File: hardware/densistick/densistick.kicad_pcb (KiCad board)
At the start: 4 copper layers, 85 x 22 mm, 66 parts, among them J1 Cable, SW1 SW_Push, U1 TSL2585, U2 USBLC6-2SC6, U3 MIC4812, U4 FT260Q, U5 MIC5365-1.8YC5, U6 CAT24C08, U7 MCP4017-104E/LT

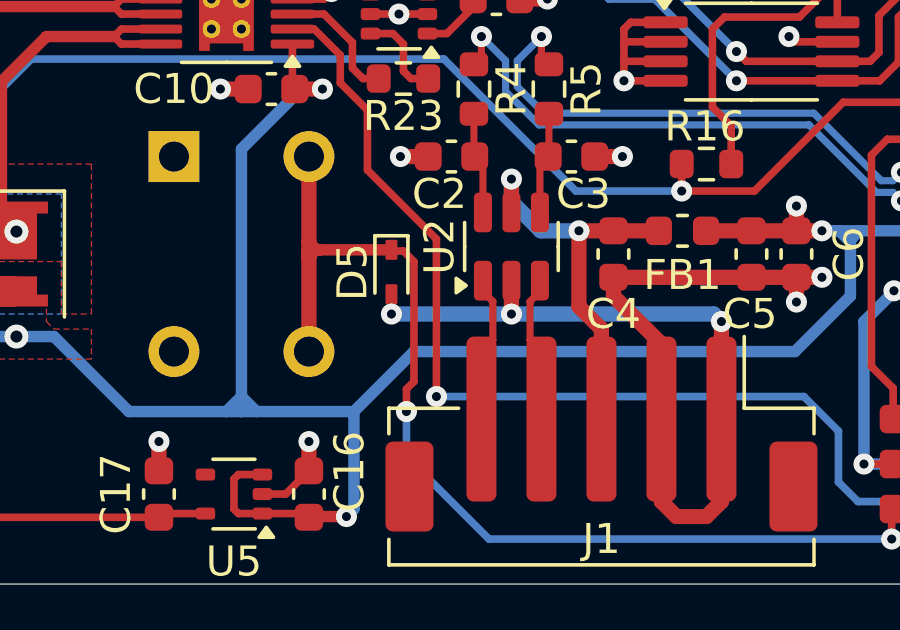
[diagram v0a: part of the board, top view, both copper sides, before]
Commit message: Update ESD diode symbols and footprints
Fix #78
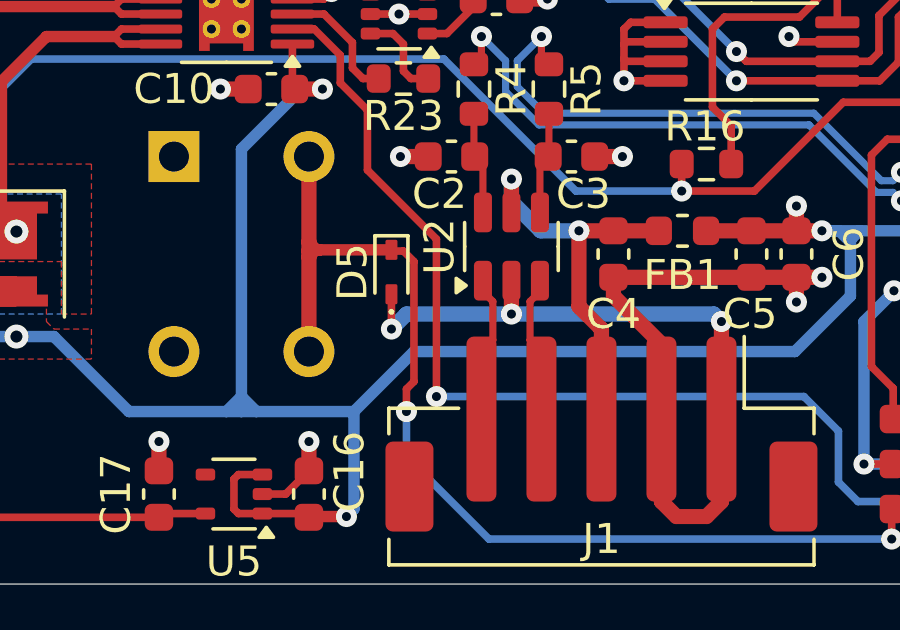
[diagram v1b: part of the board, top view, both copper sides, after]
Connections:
- D5 pad 1: Net-(D5-K) -> Earth
- D5 pad 2: Earth -> Net-(D5-K)
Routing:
- net Earth: track 19.6 -> 20.3 mm
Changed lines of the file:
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@@
 		(layer "F.Cu")
 		(at 88 68.6 -90)
-		(descr "https://www.ti.com/lit/ml/mpss124a/mpss124a.pdf")
+		(descr "https://www.ti.com/lit/ml/mpss124a/mpss124a.pdf, anode and cathod pins reversed")
 		(tags "Diode SOD523 TI DYA0002A")
 		(property "Reference" "D5"
@@
 			)
 		)
-		(property "Datasheet" "https://www.ti.com/lit/ds/slvsen8b/slvsen8b.pdf"
+		(property "Datasheet" "https://www.ti.com/lit/ds/symlink/esd321.pdf"
 			(at 0 0 -90)
 			(unlocked yes)
@@
 		(sheetname "Root")
 		(sheetfile "densistick.kicad_sch")
-		(solder_paste_margin -0.025)
 		(attr smd)
 		(fp_line
@@
 			(layer "F.SilkS")
 		)
+		(fp_circle
+			(center 1.325 0)
+			(end 1.375 0)
+			(stroke
+				(width 0.1)
+				(type solid)
+			)
+			(fill none)
+			(layer "F.SilkS")
+		)
 		(fp_line
 			(start -1.25 0.65)
@@
 		)
 		(pad "1" smd roundrect
-			(at -0.74 0 90)
+			(at 0.74 0 90)
 			(size 0.67 0.4)
 			(layers "F.Cu" "F.Paste" "F.Mask")
 			(roundrect_rratio 0.125)
-			(net 7 "Net-(D5-K)")
-			(pinfunction "K")
+			(net 21 "Earth")
+			(pinfunction "A")
 			(pintype "passive")
 		)
 		(pad "2" smd roundrect
-			(at 0.74 0 90)
+			(at -0.74 0 90)
 			(size 0.67 0.4)
 			(layers "F.Cu" "F.Paste" "F.Mask")
 			(roundrect_rratio 0.125)
-			(net 21 "Earth")
-			(pinfunction "A")
+			(net 7 "Net-(D5-K)")
+			(pinfunction "K")
 			(pintype "passive")
 		)
@@
 			)
 			(rotate
-				(xyz 0 0 0)
+				(xyz 0 0 -180)
 			)
 		)
@@
 		(layer "F.Cu")
 		(at 88.25 60 180)
-		(descr "SOT-363, SC-70-6")
-		(tags "SOT-363 SC-70-6")
+		(descr "SOT-363, SC-70-6, SC-88")
+		(tags "SOT-363 SC-70-6 SC-88")
 		(property "Reference" "U7"
 			(at 0 2 0)
@@
 		(layer "F.Cu")
 		(at 92 67.75 90)
-		(descr "SOT, 6 Pin (https://www.jedec.org/sites/default/files/docs/Mo-178c.PDF variant AB), generated with kicad-footprint-generator ipc_gullwing_generator.py")
+		(descr "SOT, 6 Pin (~), generated with kicad-footprint-generator ipc_gullwing_generator.py")
 		(tags "SOT TO_SOT_SMD")
 		(property "Reference" "U2"
@@
 	(segment
 		(start 88 69.34)
-		(end 88 70)
+		(end 88 70.5)
 		(width 0.254)
 		(layer "F.Cu")
@@
 	)
 	(via
-		(at 88 70)
+		(at 88 70.5)
 		(size 0.7)
 		(drill 0.3)
@@
 	)
 	(segment
-		(start 88 70)
-		(end 92 70)
+		(start 88 70.5)
+		(end 88.5 70)
 		(width 0.508)
 		(layer "B.Cu")
@@
 	)
 	(segment
+		(start 88.5 70)
+		(end 92 70)
+		(width 0.508)
+		(layer "B.Cu")
+		(net 21)
+	)
+	(segment
 		(start 92 70)
 		(end 98.75 70)
@@
 	)
 	(zone
-		(net 7)
-		(net_name "Net-(D5-K)")
+		(net 6)
+		(net_name "/RLED2")
 		(layer "F.Cu")
-		(name "$teardrop_padvia$")
-		(hatch full 0.1)
-		(priority 30001)
-		(attr
-			(teardrop
-				(type padvia)
-			)
-		)
+		(hatch edge 0.5)
+		(priority 6)
 		(connect_pads yes
-			(clearance 0)
+			(clearance 0.508)
 		)
-		(min_thickness 0.0254)
+		(min_thickness 0.25)
 		(filled_areas_thickness no)
 		(fill yes
 			(thermal_gap 0.5)
 			(thermal_bridge_width 0.5)
-			(island_removal_mode 1)
-			(island_area_min 10)
 		)
 		(polygon
 			(pts
-				(xy 84.996 66.45) (xy 85.504 66.45) (xy 86.035298 65.075281) (xy 85.25 64.749) (xy 84.464702 65.075281)
+				(xy 77 70) (xy 78 70) (xy 78 65) (xy 72 65) (xy 72 70) (xy 73 70) (xy 73 68.25) (xy 77 68.25)
 			)
 		)
 	)
 	(zone
-		(net 6)
-		(net_name "/RLED2")
+		(net 7)
+		(net_name "Net-(D5-K)")
 		(layer "F.Cu")
-		(hatch edge 0.5)
-		(priority 6)
+		(name "$teardrop_padvia$")
+		(hatch full 0.1)
+		(priority 30000)
+		(attr
+			(teardrop
+				(type padvia)
+			)
+		)
 		(connect_pads yes
-			(clearance 0.508)
+			(clearance 0)
 		)
-		(min_thickness 0.25)
+		(min_thickness 0.0254)
 		(filled_areas_thickness no)
 		(fill yes
 			(thermal_gap 0.5)
 			(thermal_bridge_width 0.5)
+			(island_removal_mode 1)
+			(island_area_min 10)
 		)
 		(polygon
 			(pts
-				(xy 77 70) (xy 78 70) (xy 78 65) (xy 72 65) (xy 72 70) (xy 73 70) (xy 73 68.25) (xy 77 68.25)
+				(xy 85.504 69.55) (xy 84.996 69.55) (xy 84.464702 70.924719) (xy 85.25 71.251) (xy 86.035298 70.924719)
 			)
 		)
@@
 		(name "$teardrop_padvia$")
 		(hatch full 0.1)
-		(priority 30000)
+		(priority 30001)
 		(attr
 			(teardrop
@@
 		(polygon
 			(pts
-				(xy 85.504 69.55) (xy 84.996 69.55) (xy 84.464702 70.924719) (xy 85.25 71.251) (xy 86.035298 70.924719)
+				(xy 84.996 66.45) (xy 85.504 66.45) (xy 86.035298 65.075281) (xy 85.25 64.749) (xy 84.464702 65.075281)
 			)
 		)

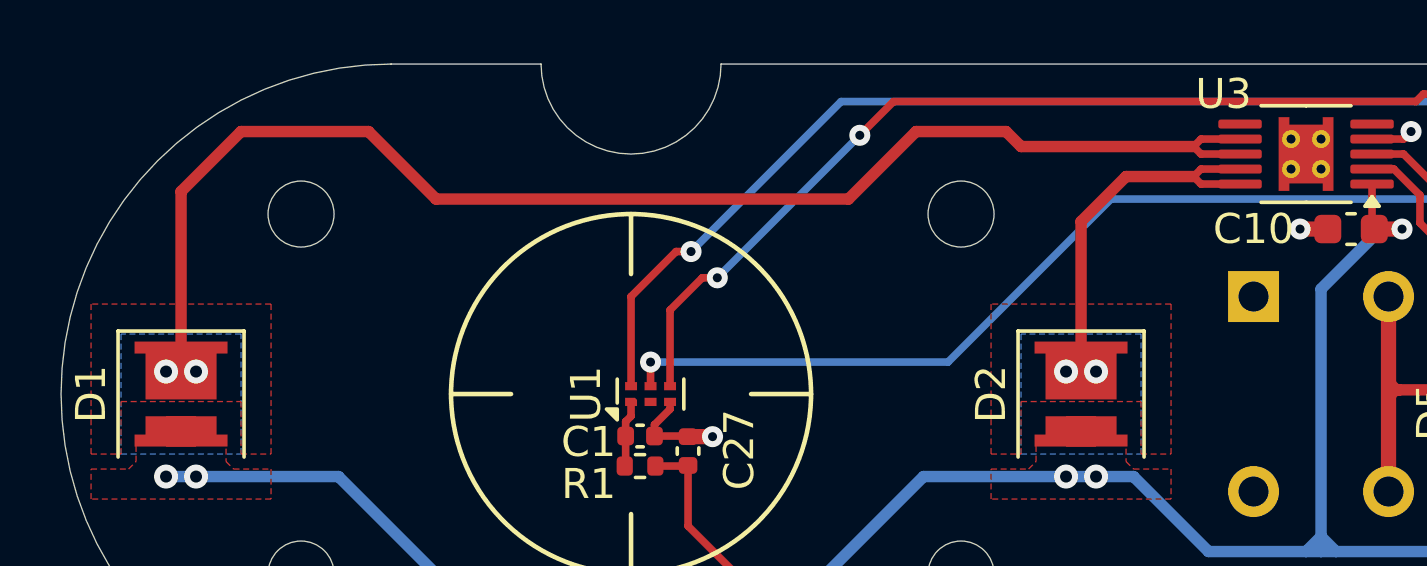
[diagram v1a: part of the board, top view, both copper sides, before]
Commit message: Change DensiStick LED driver wiring
Halve the value of the LED driver's RSET resistor, and change the LED
wiring so that channels aren't doubled.  This effect of this should be
keeping the maximum LED current the same, while halving the minimum LED
current.

Fix #80
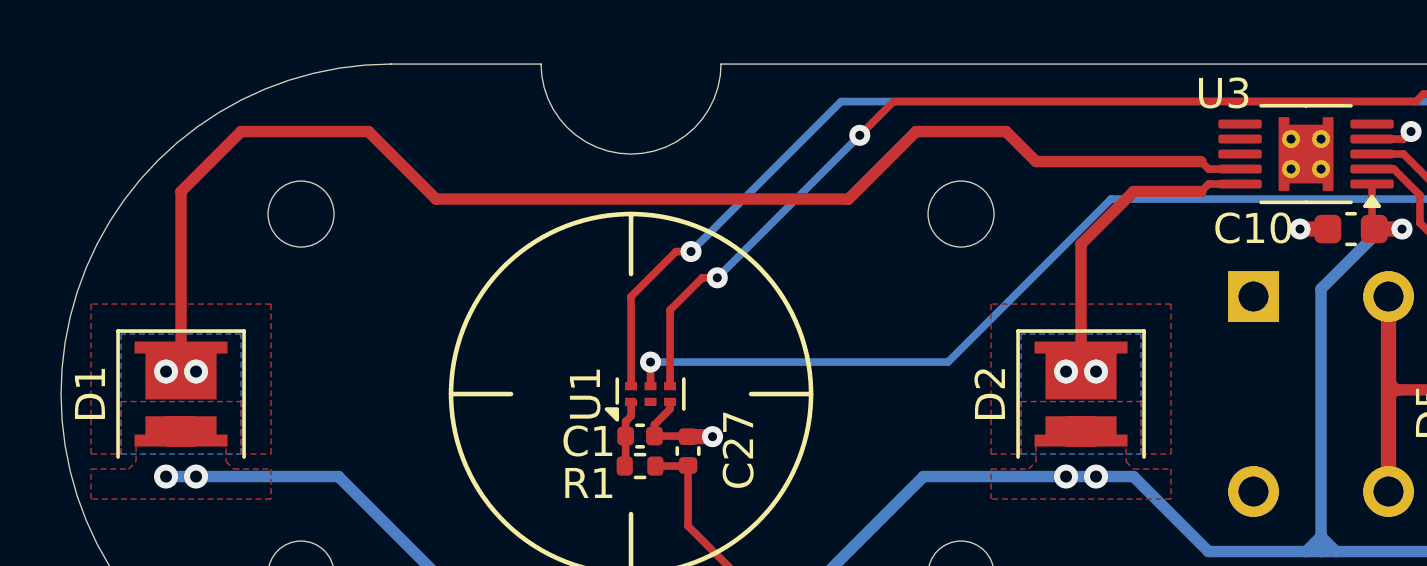
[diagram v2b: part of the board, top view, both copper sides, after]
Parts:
- R23: value 16.5k -> 8.25k
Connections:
- U3 pad 7: /RLED1 -> unconnected-(U3-D4-Pad7)
- U3 pad 8: /RLED1 -> unconnected-(U3-D3-Pad8)
- U3 pad 9: /RLED2 -> /RLED1
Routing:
- net /RLED2: track 12.8 -> 10.3 mm
- net /RLED1: track 46.1 -> 44.5 mm
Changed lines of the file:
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@@
 	(net 41 "unconnected-(U4-DIO0-Pad7)")
 	(net 42 "Net-(U7-W)")
+	(net 43 "unconnected-(U3-D4-Pad7)")
+	(net 44 "unconnected-(U3-D3-Pad8)")
 	(footprint "lib_fp:SunLike_LED_S1S0"
 		(locked yes)
@@
 			(layers "F.Cu" "F.Paste" "F.Mask")
 			(roundrect_rratio 0.25)
-			(net 5 "/RLED1")
+			(net 43 "unconnected-(U3-D4-Pad7)")
 			(pinfunction "D4")
-			(pintype "open_collector")
+			(pintype "open_collector+no_connect")
 		)
 		(pad "8" smd roundrect
@@
 			(layers "F.Cu" "F.Paste" "F.Mask")
 			(roundrect_rratio 0.25)
-			(net 5 "/RLED1")
+			(net 44 "unconnected-(U3-D3-Pad8)")
 			(pinfunction "D3")
-			(pintype "open_collector")
+			(pintype "open_collector+no_connect")
 		)
 		(pad "9" smd roundrect
@@
 			(layers "F.Cu" "F.Paste" "F.Mask")
 			(roundrect_rratio 0.25)
-			(net 6 "/RLED2")
+			(net 5 "/RLED1")
 			(pinfunction "D2")
 			(pintype "open_collector")
@@
 			)
 		)
-		(property "Value" "16.5k"
+		(property "Value" "8.25k"
 			(at 1.4 -0.1 90)
 			(layer "F.Fab")
@@
 			)
 		)
-		(property "Datasheet" "https://www.te.com/commerce/DocumentDelivery/DDEController?Action=srchrtrv&DocNm=1773200&DocType=DS&DocLang=English"
+		(property "Datasheet" "https://www.vishay.com/docs/28773/crcwce3.pdf"
 			(at 0 0 180)
 			(unlocked yes)
@@
 			)
 		)
-		(property "Description" "RES SMD 16.5K OHM 1% 1/16W 0603"
+		(property "Description" "RES SMD 8.25K OHM 1% 1/16W 0603"
 			(at 84.688 68.078 90)
 			(layer "F.Fab")
@@
 			)
 		)
-		(property "Manufacturer" "TE Connectivity Passive Product"
+		(property "Manufacturer" "Vishay Dale"
 			(at 0 0 90)
 			(layer "F.Fab")
@@
 			)
 		)
-		(property "Manufacturer PN" "CPF0603F16K5C1"
+		(property "Manufacturer PN" "CRCW06038K25FKEBC"
 			(at 0 0 90)
 			(layer "F.Fab")
@@
 			)
 		)
-		(property "Supplier" "Digi-Key"
+		(property "Supplier" "Mouser"
 			(at 0 0 90)
 			(layer "F.Fab")
@@
 			)
 		)
-		(property "Supplier PN" "A102224CT-ND"
+		(property "Supplier PN" "71-CRCW06038K25FKEBC"
 			(at 0 0 90)
 			(layer "F.Fab")
@@
 	)
 	(segment
-		(start 80.4 59.5)
-		(end 79 59.5)
-		(width 0.254)
-		(layer "F.Cu")
-		(net 5)
-	)
-	(segment
-		(start 51.25 59.25)
-		(end 47 59.25)
+		(start 69.5 59.25)
+		(end 72.5 59.25)
 		(width 0.381)
 		(layer "F.Cu")
@@
 	)
 	(segment
-		(start 79 59.5)
-		(end 78.75 59.75)
-		(width 0.254)
+		(start 73.5 60.25)
+		(end 79 60.25)
+		(width 0.381)
 		(layer "F.Cu")
 		(net 5)
 	)
 	(segment
-		(start 78.75 59.75)
-		(end 73 59.75)
+		(start 45 61.25)
+		(end 47 59.25)
 		(width 0.381)
 		(layer "F.Cu")
@@
 	(segment
 		(start 67.25 61.5)
-		(end 53.5 61.5)
+		(end 69.5 59.25)
 		(width 0.381)
 		(layer "F.Cu")
@@
 	)
 	(segment
-		(start 72.5 59.25)
-		(end 69.5 59.25)
+		(start 47 59.25)
+		(end 51.25 59.25)
 		(width 0.381)
 		(layer "F.Cu")
@@
 	)
 	(segment
-		(start 69.5 59.25)
+		(start 53.5 61.5)
 		(end 67.25 61.5)
 		(width 0.381)
@@
 	)
 	(segment
-		(start 47 59.25)
+		(start 45 67.215)
 		(end 45 61.25)
 		(width 0.381)
@@
 	)
 	(segment
-		(start 53.5 61.5)
-		(end 51.25 59.25)
-		(width 0.381)
-		(layer "F.Cu")
-		(net 5)
-	)
-	(segment
-		(start 45 61.25)
-		(end 45 67.215)
-		(width 0.381)
+		(start 79.25 60.5)
+		(end 79 60.25)
+		(width 0.254)
 		(layer "F.Cu")
 		(net 5)
 	)
 	(segment
-		(start 79 60)
-		(end 78.75 59.75)
+		(start 80.3 60.5)
+		(end 79.25 60.5)
 		(width 0.254)
 		(layer "F.Cu")
@@
 	)
 	(segment
-		(start 80.4 60)
-		(end 79 60)
-		(width 0.254)
+		(start 51.25 59.25)
+		(end 53.5 61.5)
+		(width 0.381)
 		(layer "F.Cu")
 		(net 5)
 	)
 	(segment
-		(start 73 59.75)
-		(end 72.5 59.25)
+		(start 72.5 59.25)
+		(end 73.5 60.25)
 		(width 0.381)
 		(layer "F.Cu")
@@
 	)
 	(segment
-		(start 80.4 60.5)
-		(end 79 60.5)
-		(width 0.254)
-		(layer "F.Cu")
-		(net 6)
-	)
-	(segment
-		(start 76.5 60.75)
-		(end 78.75 60.75)
+		(start 75 63)
+		(end 76.75 61.25)
 		(width 0.381)
 		(layer "F.Cu")
@@
 	)
 	(segment
-		(start 80.4 61)
-		(end 79 61)
-		(width 0.254)
-		(layer "F.Cu")
-		(net 6)
-	)
-	(segment
-		(start 79 61)
-		(end 78.75 60.75)
-		(width 0.254)
+		(start 76.75 61.25)
+		(end 79 61.25)
+		(width 0.381)
 		(layer "F.Cu")
 		(net 6)
 	)
 	(segment
-		(start 75 62.25)
-		(end 75 67.215)
+		(start 75 67.215)
+		(end 75 63)
 		(width 0.381)
 		(layer "F.Cu")
@@
 	)
 	(segment
-		(start 75 62.25)
-		(end 76.5 60.75)
-		(width 0.381)
+		(start 80.3 61)
+		(end 79.25 61)
+		(width 0.254)
 		(layer "F.Cu")
 		(net 6)
 	)
 	(segment
-		(start 79 60.5)
-		(end 78.75 60.75)
+		(start 79.25 61)
+		(end 79 61.25)
 		(width 0.254)
 		(layer "F.Cu")
@@
 		(priority 6)
 		(connect_pads yes
-			(clearance 0.508)
+			(clearance 0.25)
 		)
 		(min_thickness 0.25)
@@
 		(priority 7)
 		(connect_pads yes
-			(clearance 0.508)
+			(clearance 0.25)
 		)
 		(min_thickness 0.25)
@@
 		(priority 7)
 		(connect_pads yes
-			(clearance 0.508)
+			(clearance 0.25)
 		)
 		(min_thickness 0.25)
@@
 		(priority 6)
 		(connect_pads yes
-			(clearance 0.508)
+			(clearance 0.25)
 		)
 		(min_thickness 0.25)
@@
 		(name "$teardrop_padvia$")
 		(hatch full 0.1)
-		(priority 30000)
+		(priority 30001)
 		(attr
 			(teardrop
@@
 		(polygon
 			(pts
-				(xy 85.504 69.55) (xy 84.996 69.55) (xy 84.464702 70.924719) (xy 85.25 71.251) (xy 86.035298 70.924719)
+				(xy 84.996 66.45) (xy 85.504 66.45) (xy 86.035298 65.075281) (xy 85.25 64.749) (xy 84.464702 65.075281)
 			)
 		)
@@
 		(name "$teardrop_padvia$")
 		(hatch full 0.1)
-		(priority 30001)
+		(priority 30000)
 		(attr
 			(teardrop
@@
 		(polygon
 			(pts
-				(xy 84.996 66.45) (xy 85.504 66.45) (xy 86.035298 65.075281) (xy 85.25 64.749) (xy 84.464702 65.075281)
+				(xy 85.504 69.55) (xy 84.996 69.55) (xy 84.464702 70.924719) (xy 85.25 71.251) (xy 86.035298 70.924719)
 			)
 		)

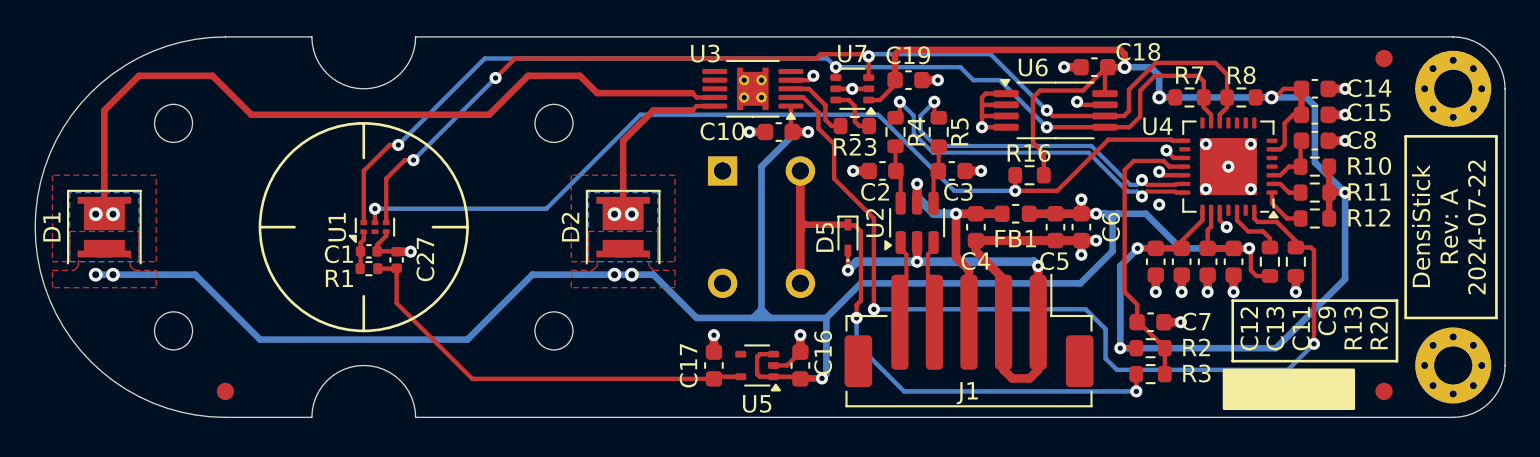
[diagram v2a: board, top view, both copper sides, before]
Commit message: Route VSYNC to FT260 GPIOA on DensiStick
This makes the sensor-to-bridge connection on the DensiStick logically
match the same from the Meter Probe, and makes it possible to experiment
with using VSYNC as a trigger.

Doing this may be useful to provide more ways of operating the sensor,
and doesn't hurt if not used.

More routing cleanup may be necessary before this design is considered
complete.
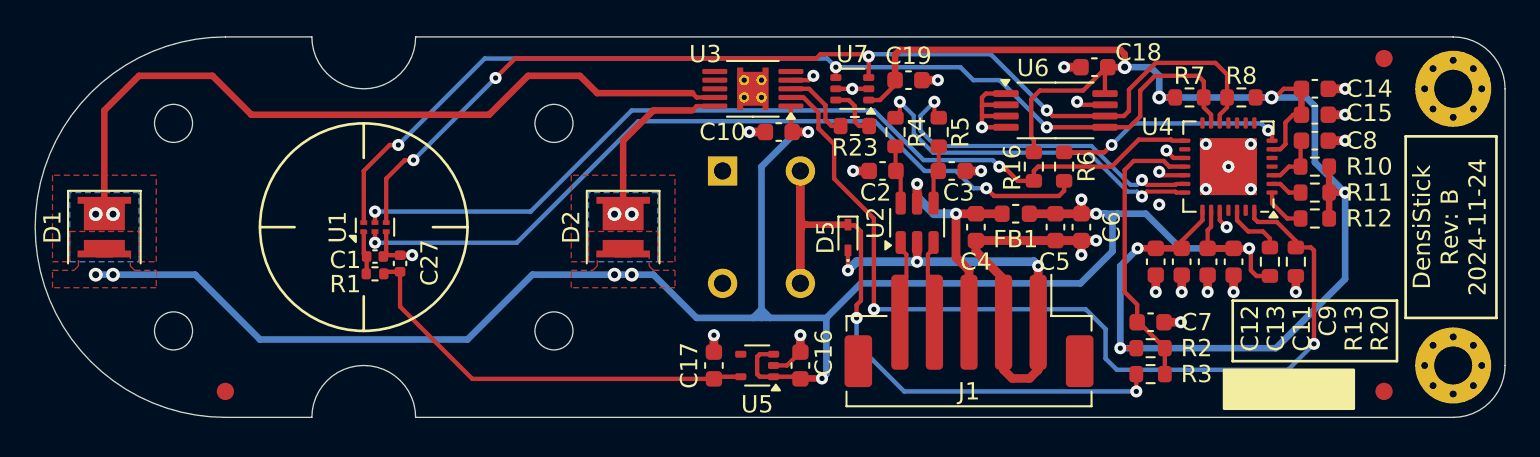
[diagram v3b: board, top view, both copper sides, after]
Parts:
- added R6: 33R, Resistor_SMD:R_0603_1608Metric, F.Cu at (100.5, 64.5)
- moved R16 0.56 mm to (98.8, 64.5), turned to -90 degrees
- moved C1 0.46 mm to (60.6, 69.7)
- moved R1 0.46 mm to (60.6, 70.7)
- moved C27 0.28 mm to (62.1, 70.1)
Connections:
- U1 pad 2: unconnected-(U1-VSYNC/GPIO-Pad2) -> /TSL_VSYNC
- U4 pad 7: unconnected-(U4-DIO0-Pad7) -> Net-(U4-DIO0)
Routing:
- net /TSL_VSYNC: track 0.00 -> 45.9 mm, vias 0 -> 2
- net Net-(U4-DIO0): track 0.00 -> 13.4 mm, vias 0 -> 2
- net +3V3: track 92.6 -> 91.1 mm
- net /TSL_INT: track 53.9 -> 52.9 mm
- net +1V8: track 24.7 -> 24.1 mm

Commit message: Finalize DensiStick Rev B 2024-12-03
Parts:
- moved C1 0.10 mm to (60.6, 69.6)
- moved R1 0.10 mm to (60.6, 70.6)
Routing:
- net /TSL_INT: track 52.9 -> 54.9 mm
- net +5V: track 116.3 -> 117.3 mm, vias 9 -> 13
- net /I2C_SCL: track 62.2 -> 62.9 mm
- net /RLED1: track 44.5 -> 44.1 mm, vias 2 -> 4
- net /RLED2: vias 2 -> 4
- added copper zone on B.Cu, net +5V
